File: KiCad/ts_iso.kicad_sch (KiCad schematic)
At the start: 70 parts, among them U17 PEME1-S5-S5-S, U18 PEME1-S5-S5-S, U19 TL431DBZ, U20 ACPL-C87B, U21 ACPL-C87B, U22 LTV-817S, U23 OPA4342EA

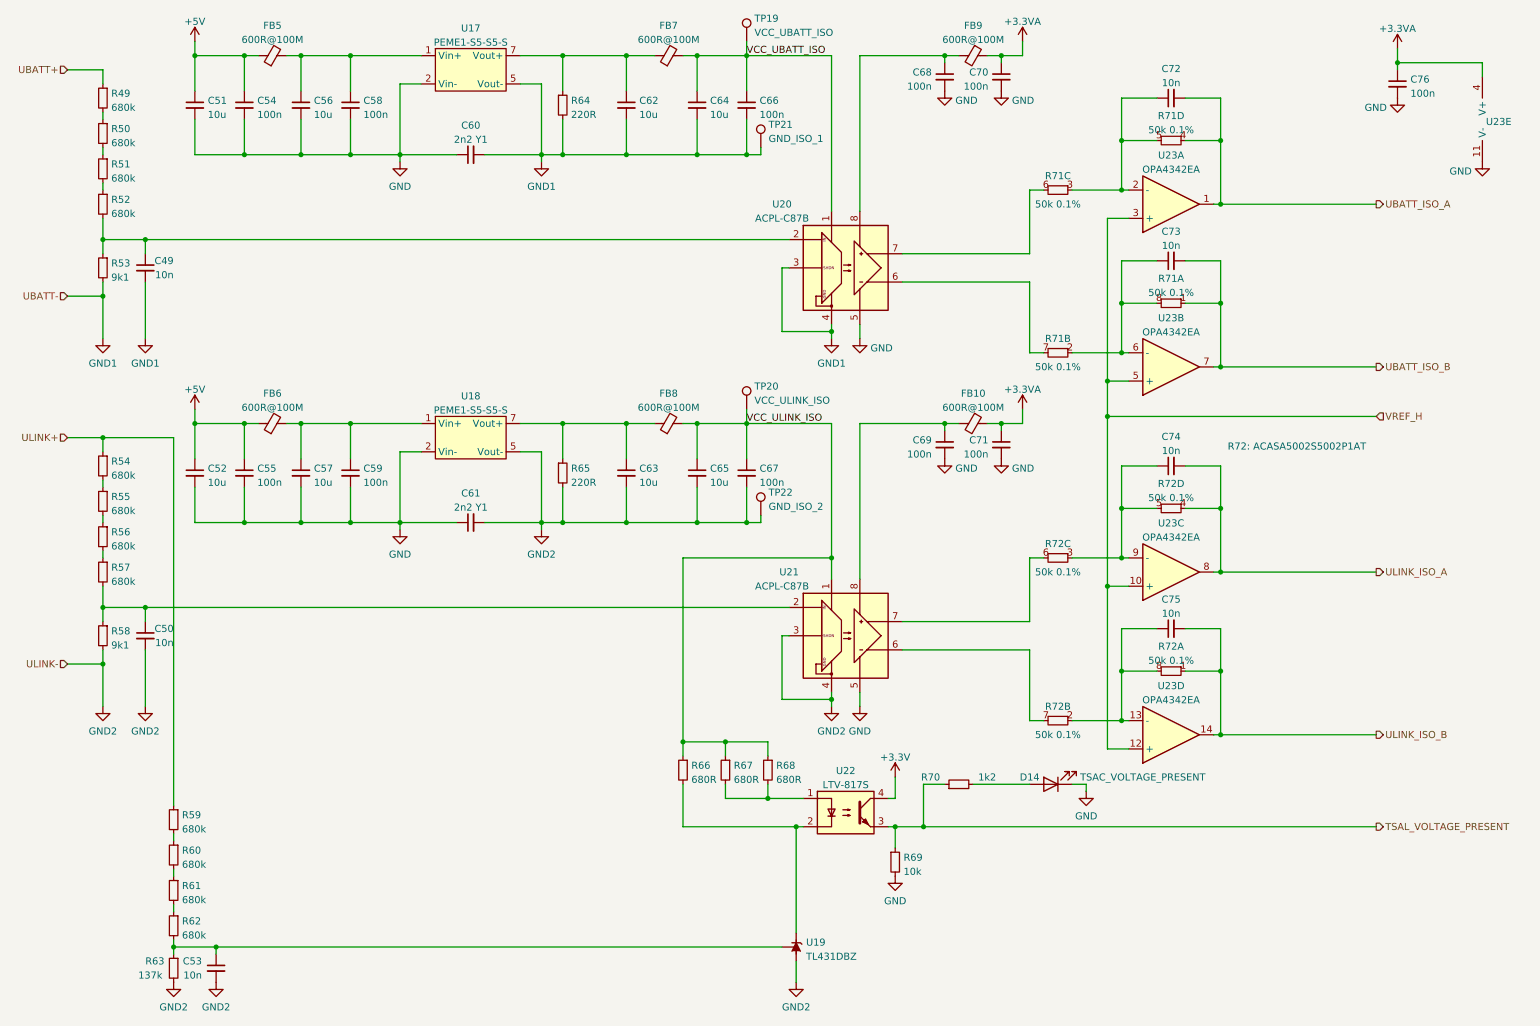
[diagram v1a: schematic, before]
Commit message: Update KiCad project to newest version
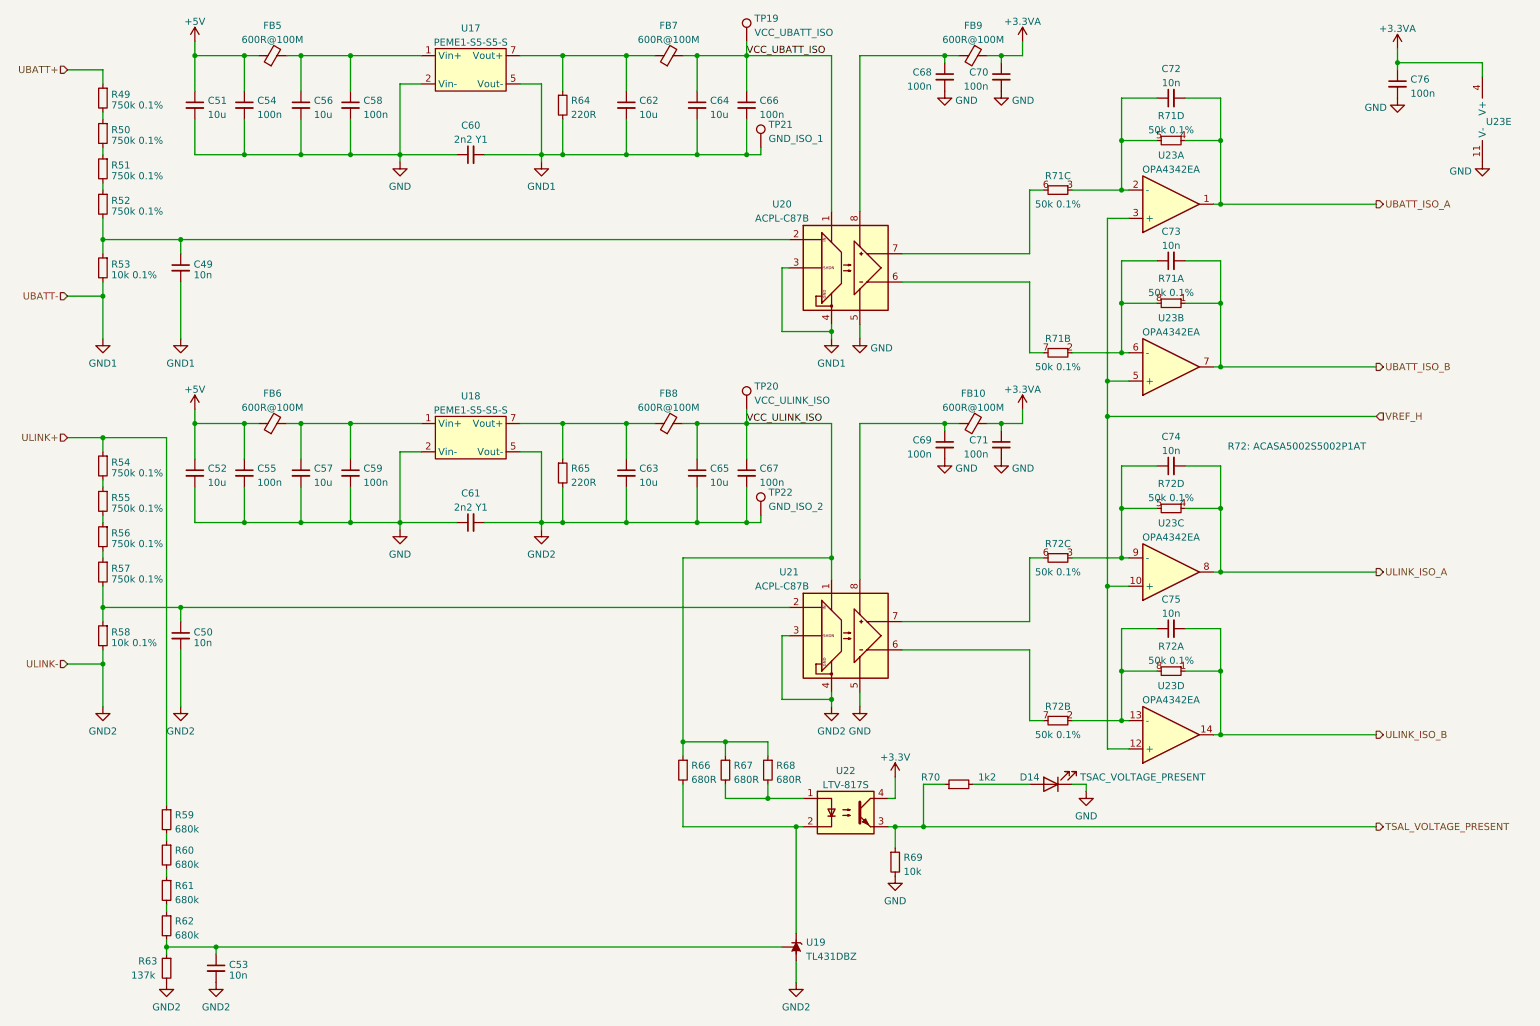
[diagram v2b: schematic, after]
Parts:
- R49, R50, R51, R52, R54, R55, R56, R57: value 680k -> 750k 0.1%
- R53, R58: value 9k1 -> 10k 0.1%
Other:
- moved on the sheet: C49, C50, R59, R60, R61, R62, R63
